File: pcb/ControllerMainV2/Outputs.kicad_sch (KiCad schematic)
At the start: 30 parts, among them IC20 TMUX6112PWR, IC27 1462039-4, Q5 2N7002, Q7 EL817S1_A__TU_-F, T1 Lehle_MZ_P, U12 TL072

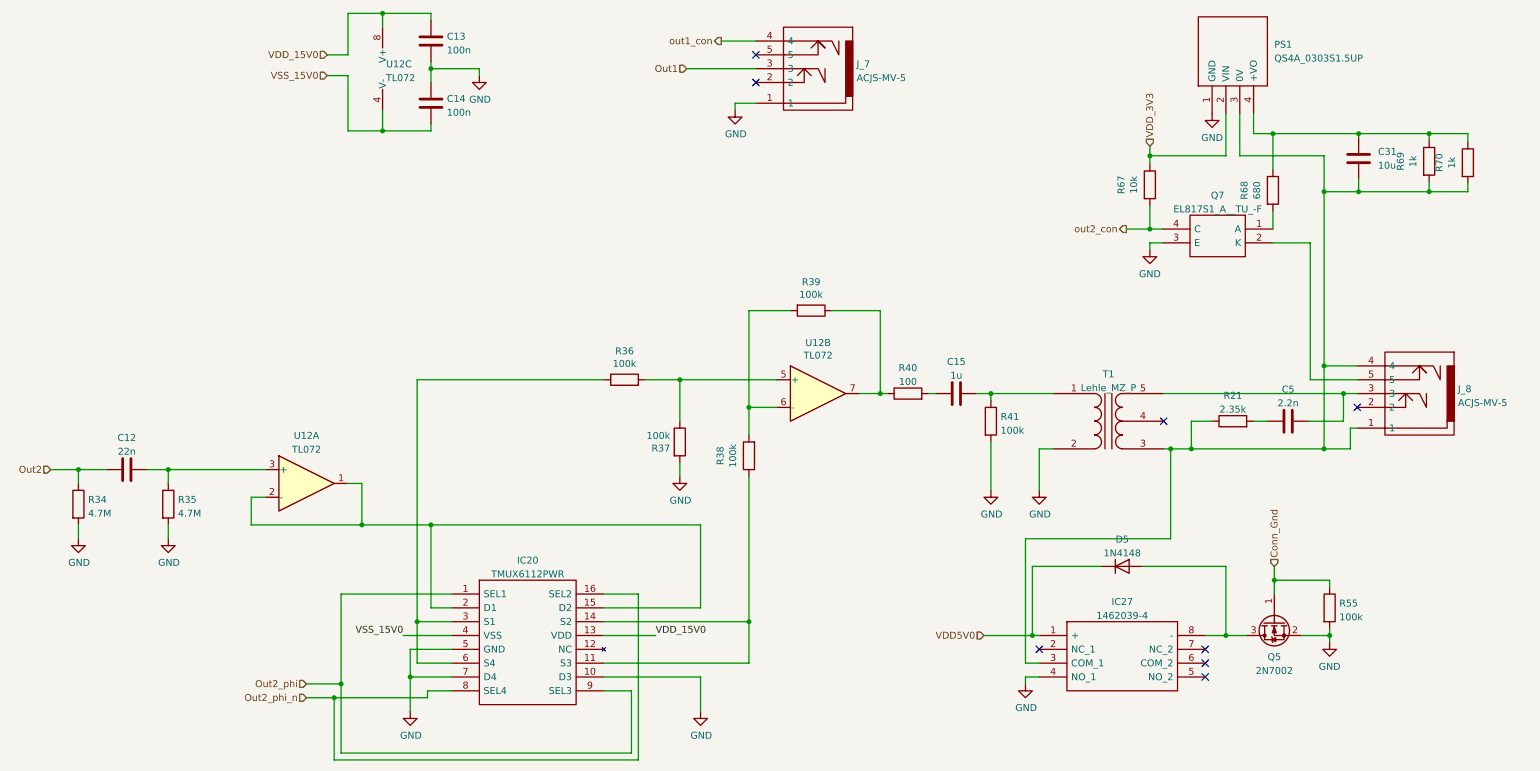
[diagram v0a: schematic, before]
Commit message: New version with smaller enclosure
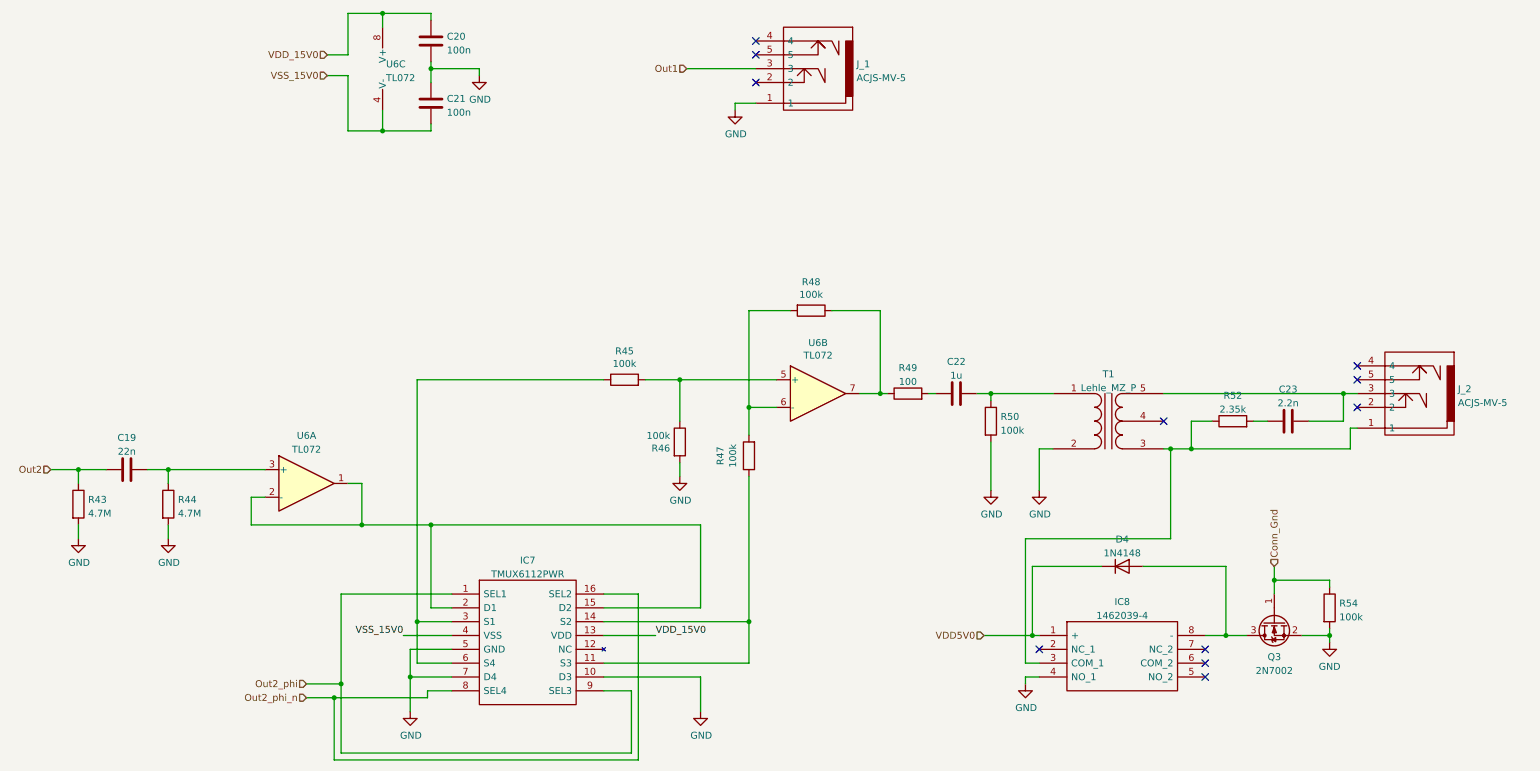
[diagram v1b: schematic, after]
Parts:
- removed C31: 10u, Capacitor_SMD:C_1206_3216Metric_Pad1.33x1.80mm_HandSolder, symbol Device:C
- removed PS1: QS4A_0303S1.5UP, SamacSys_Parts:QS4A_1.5UP, symbol SamacSys_Parts:QS4A_0303S1.5UP
- removed Q7: EL817S1_A__TU_-F, SamacSys_Parts:SOP254P1030X390-4N, symbol SamacSys_Parts:EL817S1_A__TU_-F
- removed R67: 10k, Resistor_SMD:R_1206_3216Metric_Pad1.30x1.75mm_HandSolder, symbol Device:R
- removed R68: 680, Resistor_SMD:R_1206_3216Metric_Pad1.30x1.75mm_HandSolder, symbol Device:R
- removed R69, R70: 1k, Resistor_SMD:R_1206_3216Metric_Pad1.30x1.75mm_HandSolder, symbol Device:R
- R43: renamed from R34; footprint Resistor_SMD:R_1206_3216Metric_Pad1.30x1.75mm_HandSolder -> Resistor_SMD:R_0805_2012Metric_Pad1.20x1.40mm_HandSolder
- R44: renamed from R35; footprint Resistor_SMD:R_1206_3216Metric_Pad1.30x1.75mm_HandSolder -> Resistor_SMD:R_0805_2012Metric_Pad1.20x1.40mm_HandSolder
- R45: renamed from R36; footprint Resistor_SMD:R_1206_3216Metric_Pad1.30x1.75mm_HandSolder -> Resistor_SMD:R_0805_2012Metric_Pad1.20x1.40mm_HandSolder
- R46: renamed from R37; footprint Resistor_SMD:R_1206_3216Metric_Pad1.30x1.75mm_HandSolder -> Resistor_SMD:R_0805_2012Metric_Pad1.20x1.40mm_HandSolder
- R47: renamed from R38; footprint Resistor_SMD:R_1206_3216Metric_Pad1.30x1.75mm_HandSolder -> Resistor_SMD:R_0805_2012Metric_Pad1.20x1.40mm_HandSolder
- R48: renamed from R39; footprint Resistor_SMD:R_1206_3216Metric_Pad1.30x1.75mm_HandSolder -> Resistor_SMD:R_0805_2012Metric_Pad1.20x1.40mm_HandSolder
- R49: renamed from R40; footprint Resistor_SMD:R_1206_3216Metric_Pad1.30x1.75mm_HandSolder -> Resistor_SMD:R_0805_2012Metric_Pad1.20x1.40mm_HandSolder
- R50: renamed from R41; footprint Resistor_SMD:R_1206_3216Metric_Pad1.30x1.75mm_HandSolder -> Resistor_SMD:R_0805_2012Metric_Pad1.20x1.40mm_HandSolder
- R52: renamed from R21; footprint Resistor_SMD:R_1206_3216Metric_Pad1.30x1.75mm_HandSolder -> Resistor_SMD:R_0805_2012Metric_Pad1.20x1.40mm_HandSolder
- R54: renamed from R55; footprint Resistor_SMD:R_1206_3216Metric_Pad1.30x1.75mm_HandSolder -> Resistor_SMD:R_0805_2012Metric_Pad1.20x1.40mm_HandSolder
- U6: renamed from U12; footprint SamacSys_Parts:SOIC127P600X175-8N -> Package_SO:SOIC-8_3.9x4.9mm_P1.27mm
- renumbered C12 to C19, C13 to C20, C14 to C21, C15 to C22, C5 to C23, D5 to D4, IC20 to IC7, IC27 to IC8, J_7 to J_1, J_8 to J_2, Q5 to Q3
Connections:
- net at IC8.3 (COM_1), J_2.1, R52.1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: no longer J_2.4
- net out1_con: no longer names the net of J_1.4
- no-connect marks 8 -> 11
